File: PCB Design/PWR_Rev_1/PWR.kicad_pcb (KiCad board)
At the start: 2 copper layers, 40 x 65 mm, 61 parts, among them J1 Conn_01x24_Pin, J2 Conn_01x24_Pin, U1 LMR33630ADDA, U2 LMR33630ADDA, U3 LMR33630ADDA

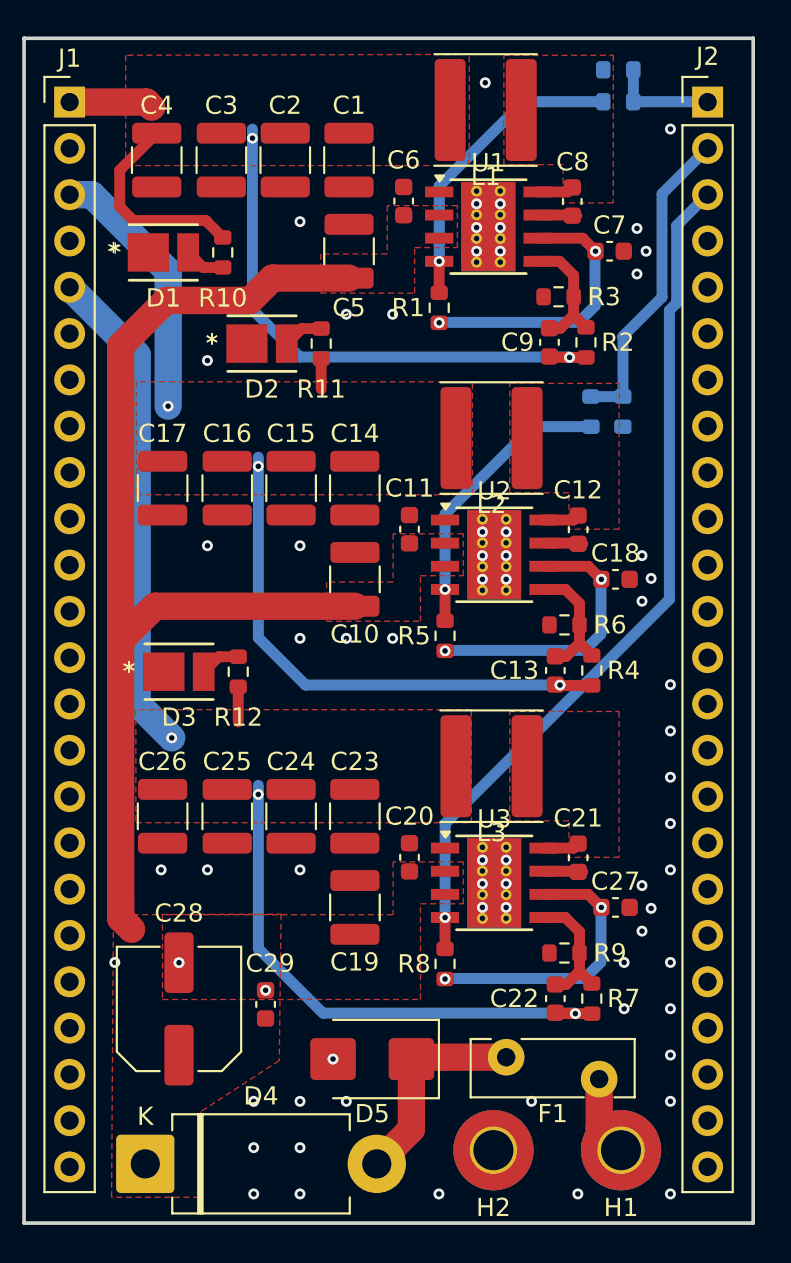
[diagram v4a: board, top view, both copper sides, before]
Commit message: Added Boost for V_Piezo
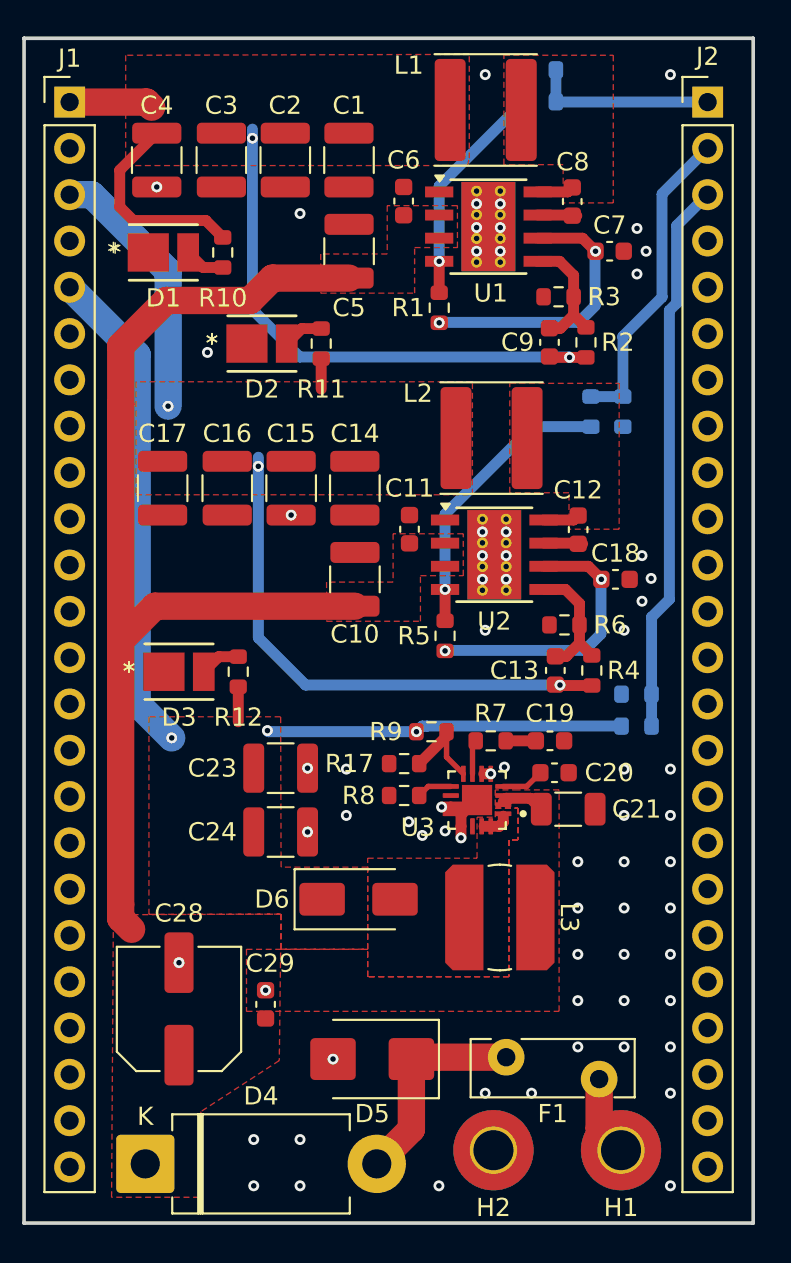
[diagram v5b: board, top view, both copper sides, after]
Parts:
- removed C22: C, Capacitor_SMD:C_0603_1608Metric
- removed C25, C26: 22u, Capacitor_SMD:C_1210_3225Metric
- removed C27: 1u, Capacitor_SMD:C_0603_1608Metric
- added D6: SS34-HF, Diode_SMD:D_SMA, F.Cu at (152.2, 115.8)
- added R17: 10k, Resistor_SMD:R_0603_1608Metric, F.Cu at (154.8, 108.3)
- added R18: 182k, Resistor_SMD:R_0603_1608Metric, B.Cu at (167.5, 106.2)
- added R19: 10k, Resistor_SMD:R_0603_1608Metric, B.Cu at (167.5, 104.5)
- C19: value 10u -> 10n; footprint Capacitor_SMD:C_1210_3225Metric -> Capacitor_SMD:C_0603_1608Metric
- C20: value 0.22u -> 100n
- C21: value 0.1u -> 10u; footprint Capacitor_SMD:C_0603_1608Metric -> Capacitor_SMD:C_1206_3216Metric
- L3: value N/A -> 22u; footprint PWR_Library:L_Wuerth_MAPI-5030 -> Inductor_SMD:L_Bourns_SDR0604
- R7: value N/A -> 10k
- R8: value 100k -> 84.5k
- R9: value N/A -> 187k
- U3: value LMR33630ADDA -> TPS55340RTER; footprint PWR_Library:Texas_HSOP-8-1EP_3.9x4.9mm_P1.27mm_ThermalVias -> PWR_Library:QFN50P300X300X80-17N
- moved R7 15.2 mm to (159.5, 107.1), turned to 180 degrees
- moved R9 14.2 mm to (156.2, 106.6), turned to 180 degrees
- moved C19 14.1 mm to (162.8, 107.1), turned to 0 degrees
- moved R8 9.51 mm to (154.8, 110.1), turned to 0 degrees
- moved C20 9.21 mm to (163.0, 108.8), turned to 0 degrees
- moved L3 8.31 mm to (160.0, 116.8), turned to -90 degrees
- moved C23 4.85 mm to (148.0, 108.6), turned to 0 degrees
- moved U3 4.64 mm to (158.8, 110.3), turned to 180 degrees
- moved R13 4.25 mm to (162.2, 72.0)
- moved R14 4.25 mm to (162.2, 70.2)
- moved C21 2.72 mm to (163.8, 110.8), turned to 0 degrees
- moved C24 1.03 mm to (148.0, 112.1), turned to 0 degrees
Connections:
- C19 pad 1: VIN -> Net-(C19-Pad1)
- C20 pad 1: VIN -> Net-(U3-SS)
- C21 pad 1: Net-(U3-SW) -> VIN
- C21 pad 2: Net-(U3-BOOT) -> GND
- L3 pad 1: Net-(U3-SW) -> VIN
- L3 pad 2: V_Piezo -> Net-(D6-A)
- R7 pad 1: Net-(U3-FB) -> Net-(C19-Pad1)
- R7 pad 2: V_Piezo -> Net-(U3-COMP)
- R8 pad 1: /PG_VPiezo_IC -> GND
- R8 pad 2: Net-(U3-VCC) -> Net-(U3-FREQ)
- R9 pad 1: GND -> Net-(U3-FB)
- R9 pad 2: Net-(U3-FB) -> V_Piezo
- U3 pad 1: GND -> Net-(D6-A)
- U3 pad 4: /PG_VPiezo_IC -> Net-(U3-SS)
- U3 pad 5: Net-(U3-FB) -> GND
- U3 pad 6: Net-(U3-VCC) -> GND
- U3 pad 7: Net-(U3-BOOT) -> Net-(U3-COMP)
- U3 pad 8: Net-(U3-SW) -> Net-(U3-FB)
- U3 pad 9: GND -> Net-(U3-FREQ)
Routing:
- net /PG_VPiezo: track 47.3 -> 30.4 mm, vias 1 -> 0
- net Net-(U3-VCC): track 15.4 -> 0.00 mm, vias 2 -> 0
- net V_Piezo: track 58.8 -> 48.5 mm
- net GND: track 0.00 -> 4.96 mm, vias 67 -> 68
- net /PG_3.3V_IC: track 16.8 -> 12.4 mm
- net /PG_3.3V: track 5.83 -> 10.1 mm
- net VIN: track 60.0 -> 62.5 mm
- net Net-(U3-SS): track 0.00 -> 2.35 mm
- net Net-(U3-SW): track 2.00 -> 0.00 mm
- net Net-(U3-FB): track 7.05 -> 5.06 mm
- net Net-(U3-BOOT): track 1.96 -> 0.00 mm
- net Net-(U3-FREQ): track 0.00 -> 1.94 mm
- net Net-(U3-COMP): track 0.00 -> 1.88 mm
- net Net-(C19-Pad1): track 0.00 -> 1.65 mm
- net Net-(D6-A): track 0.00 -> 1.49 mm
- added copper zone on F.Cu, net Net-(D6-A)
- removed copper zone on F.Cu, net Net-(U3-SW)

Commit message: Updated
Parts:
- added J1: Conn_02x25_Odd_Even, CONTROL:HIROSE_DF40C-50DP-0.4V_51_, F.Cu at (208.7, 73.0)
- added J2: Conn_02x25_Odd_Even, CONTROL:HIROSE_DF40C-50DP-0.4V_51_, F.Cu at (242.7, 73.0)
- added J3: Conn_02x25_Odd_Even, CONTROL:HIROSE_DF40C-50DP-0.4V_51_, B.Cu at (208.7, 73.0)
- added J4: Conn_02x25_Odd_Even, CONTROL:HIROSE_DF40C-50DP-0.4V_51_, B.Cu at (242.7, 73.0)
- added REF**: MountingHole_2.2mm_M2, MountingHole:MountingHole_2.2mm_M2, F.Cu at (242.7, 58.0)
- added REF**: MountingHole_2.2mm_M2, MountingHole:MountingHole_2.2mm_M2, F.Cu at (242.7, 88.0)
- added REF**: MountingHole_2.2mm_M2, MountingHole:MountingHole_2.2mm_M2, F.Cu at (208.7, 88.0)
- added REF**: MountingHole_2.2mm_M2, MountingHole:MountingHole_2.2mm_M2, F.Cu at (208.7, 58.0)
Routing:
- net /SDA: track 0.00 -> 5.42 mm, vias 0 -> 3
- net /SCL: track 0.00 -> 5.42 mm, vias 0 -> 3
- net /PC9: track 0.00 -> 5.42 mm, vias 0 -> 3
- net /PC8: track 0.00 -> 5.42 mm, vias 0 -> 3
- net /PC7: track 0.00 -> 5.42 mm, vias 0 -> 3
- net /PC6: track 0.00 -> 5.42 mm, vias 0 -> 3
- net /PC5: track 0.00 -> 5.42 mm, vias 0 -> 3
- net /PC4: track 0.00 -> 5.42 mm, vias 0 -> 3
- net /PC3: track 0.00 -> 5.42 mm, vias 0 -> 3
- net /PC13: track 0.00 -> 5.42 mm, vias 0 -> 3
- net /PC0: track 0.00 -> 5.42 mm, vias 0 -> 3
- net /PB6: track 0.00 -> 5.42 mm, vias 0 -> 3
- net /PB5: track 0.00 -> 5.42 mm, vias 0 -> 3
- net /PB15: track 0.00 -> 5.42 mm, vias 0 -> 3
- net /PB14: track 0.00 -> 5.42 mm, vias 0 -> 3
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- added copper zone on B.Cu, net 3.3V
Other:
- board size 40 x 65 mm -> 111.8 x 90.5 mm
- board text added: "BOARD TITLE REV2.0 05/2026 By S. Chong"

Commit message: Revert "Updated"
This reverts commit 89be44ed720659141c8ee702c54a520a60db740f.
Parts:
- removed the J1 at (208.7, 73.0)
- removed the J2 at (242.7, 73.0)
- removed J3, J4: Conn_02x25_Odd_Even, CONTROL:HIROSE_DF40C-50DP-0.4V_51_
- removed REF** (x4): MountingHole_2.2mm_M2, MountingHole:MountingHole_2.2mm_M2
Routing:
- net /SDA: track 5.42 -> 0.00 mm, vias 3 -> 0
- net /SCL: track 5.42 -> 0.00 mm, vias 3 -> 0
- net /PC9: track 5.42 -> 0.00 mm, vias 3 -> 0
- net /PC8: track 5.42 -> 0.00 mm, vias 3 -> 0
- net /PC7: track 5.42 -> 0.00 mm, vias 3 -> 0
- net /PC6: track 5.42 -> 0.00 mm, vias 3 -> 0
- net /PC5: track 5.42 -> 0.00 mm, vias 3 -> 0
- net /PC4: track 5.42 -> 0.00 mm, vias 3 -> 0
- net /PC3: track 5.42 -> 0.00 mm, vias 3 -> 0
- net /PC13: track 5.42 -> 0.00 mm, vias 3 -> 0
- net /PC0: track 5.42 -> 0.00 mm, vias 3 -> 0
- net /PB6: track 5.42 -> 0.00 mm, vias 3 -> 0
- net /PB5: track 5.42 -> 0.00 mm, vias 3 -> 0
- net /PB15: track 5.42 -> 0.00 mm, vias 3 -> 0
- net /PB14: track 5.42 -> 0.00 mm, vias 3 -> 0
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- removed copper zone on B.Cu, net 3.3V
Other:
- board size 111.8 x 90.5 mm -> 40 x 65 mm
- board text removed: "BOARD TITLE REV2.0 05/2026 By S. Chong"
